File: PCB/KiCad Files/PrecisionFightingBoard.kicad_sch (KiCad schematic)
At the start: 14 parts, among them J1 Conn_01x04_Male, J10 ST01x05, J2 Screw_Terminal_01x04, J3 Conn_01x14_Socket, J4 Conn_01x14_Socket, J6 Conn_02x10_Odd_Even, J7 ST01x05, J8 ST01x05, J9 ST01x05, U1 Teensy4.0

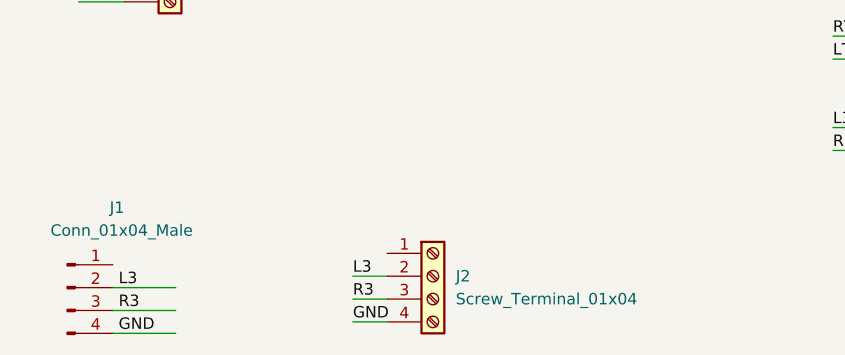
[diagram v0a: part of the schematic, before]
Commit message: Changed 4-pin screw terminal to 3-pin.
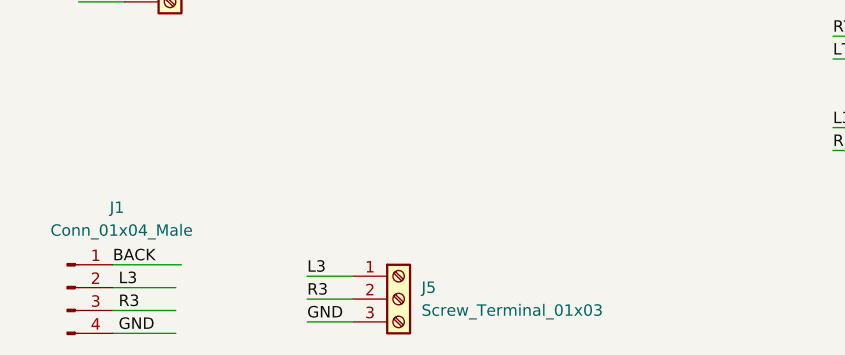
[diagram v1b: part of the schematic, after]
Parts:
- removed J2: Screw_Terminal_01x04, TerminalBlock_MetzConnect:TerminalBlock_MetzConnect_Type059_RT06304HBWC_1x04_P3.50mm_Horizontal, symbol Connector:Screw_Terminal_01x04
- added J5: Screw_Terminal_01x03, symbol Connector:Screw_Terminal_01x03
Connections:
- net BACK: now also J1.1 (Pin_1)
- net GND: now also J5.3 (Pin_3)
- net L3: now also J5.1 (Pin_1)
- net R3: now also J5.2 (Pin_2)
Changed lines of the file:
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@@
     (stroke (width 0) (type default))
   )
-  (wire (pts (xy 60.96 102.87) (xy 64.77 102.87))
+  (wire (pts (xy 55.88 102.87) (xy 60.96 102.87))
     (stroke (width 0) (type default))
   )
@@
     (stroke (width 0) (type default))
   )
+  (wire (pts (xy 55.88 100.33) (xy 60.96 100.33))
+    (stroke (width 0) (type default))
+  )
   (wire (pts (xy 92.71 40.64) (xy 85.09 40.64))
     (stroke (width 0) (type default))
@@
     (stroke (width 0) (type default))
   )
+  (wire (pts (xy 55.88 105.41) (xy 60.96 105.41))
+    (stroke (width 0) (type default))
+  )
   (wire (pts (xy 63.5 45.72) (xy 72.39 45.72))
     (stroke (width 0) (type default))
@@
     (stroke (width 0) (type default))
   )
+  (wire (pts (xy 34.29 99.06) (xy 41.91 99.06))
+    (stroke (width 0) (type default))
+  )
   (wire (pts (xy 92.71 53.34) (xy 85.09 53.34))
     (stroke (width 0) (type default))
@@
     (stroke (width 0) (type default))
   )
-  (wire (pts (xy 60.96 100.33) (xy 64.77 100.33))
-    (stroke (width 0) (type default))
-  )
   (wire (pts (xy 35.56 69.85) (xy 30.48 69.85))
     (stroke (width 0) (type default))
@@
     (stroke (width 0) (type default))
   )
-  (wire (pts (xy 60.96 105.41) (xy 64.77 105.41))
-    (stroke (width 0) (type default))
-  )
   (label "START" (at 31.115 44.45 0) (fields_autoplaced)
     (effects (font (size 1.27 1.27)) (justify left bottom))
   )
+  (label "GND" (at 55.88 105.41 0) (fields_autoplaced)
+    (effects (font (size 1.27 1.27)) (justify left bottom))
+  )
   (label "X" (at 180.34 41.91 0) (fields_autoplaced)
     (effects (font (size 1.27 1.27)) (justify left bottom))
@@
     (effects (font (size 1.27 1.27)) (justify left bottom))
   )
+  (label "R3" (at 55.88 102.87 0) (fields_autoplaced)
+    (effects (font (size 1.27 1.27)) (justify left bottom))
+  )
   (label "DOWN" (at 180.34 26.67 0) (fields_autoplaced)
     (effects (font (size 1.27 1.27)) (justify left bottom))
@@
     (effects (font (size 1.27 1.27)) (justify left bottom))
   )
+  (label "BACK" (at 34.29 99.06 0) (fields_autoplaced)
+    (effects (font (size 1.27 1.27)) (justify left bottom))
+  )
   (label "RT" (at 213.36 52.07 0) (fields_autoplaced)
     (effects (font (size 1.27 1.27)) (justify left bottom))
@@
     (effects (font (size 1.27 1.27)) (justify left bottom))
   )
-  (label "R3" (at 60.96 102.87 0) (fields_autoplaced)
-    (effects (font (size 1.27 1.27)) (justify left bottom))
-  )
   (label "BACK" (at 114.3 38.1 0) (fields_autoplaced)
     (effects (font (size 1.27 1.27)) (justify left bottom))
@@
     (effects (font (size 1.27 1.27)) (justify left bottom))
   )
-  (label "L3" (at 60.96 100.33 0) (fields_autoplaced)
-    (effects (font (size 1.27 1.27)) (justify left bottom))
-  )
   (label "GND" (at 31.115 69.85 0) (fields_autoplaced)
     (effects (font (size 1.27 1.27)) (justify left bottom))
@@
     (effects (font (size 1.27 1.27)) (justify left bottom))
   )
-  (label "GND" (at 60.96 105.41 0) (fields_autoplaced)
-    (effects (font (size 1.27 1.27)) (justify left bottom))
-  )
   (label "START" (at 114.3 40.64 0) (fields_autoplaced)
     (effects (font (size 1.27 1.27)) (justify left bottom))
@@
   )
   (label "GND" (at 34.925 106.68 0) (fields_autoplaced)
+    (effects (font (size 1.27 1.27)) (justify left bottom))
+  )
+  (label "L3" (at 55.88 100.33 0) (fields_autoplaced)
     (effects (font (size 1.27 1.27)) (justify left bottom))
   )
@@
     )
   )
+  (symbol (lib_id "Connector:Screw_Terminal_01x03") (at 66.04 102.87 0) (unit 1)
+    (in_bom yes) (on_board yes) (dnp no) (fields_autoplaced)
+    (property "Reference" "J5" (at 68.58 101.6 0)
+      (effects (font (size 1.27 1.27)) (justify left))
+    )
+    (property "Value" "Screw_Terminal_01x03" (at 68.58 104.14 0)
+      (effects (font (size 1.27 1.27)) (justify left))
+    )
+    (property "Footprint" "" (at 66.04 102.87 0)
+      (effects (font (size 1.27 1.27)) hide)
+    )
+    (property "Datasheet" "~" (at 66.04 102.87 0)
+      (effects (font (size 1.27 1.27)) hide)
+    )
+    (pin "1")
+    (pin "2")
+    (pin "3")
+    (instances
+      (project "PrecisionFightingBoard"
+        (path "/01d790aa-01e7-46c4-a23c-7deb91137dd0"
+          (reference "J5") (unit 1)
+        )
+      )
+    )
+  )
   (symbol (lib_id "Connector:Conn_01x04_Male") (at 29.21 101.6 0) (unit 1)
     (in_bom yes) (on_board yes) (dnp no)
@@
         )
       )
-    )
-  )
-  (symbol (lib_id "Connector:Screw_Terminal_01x04") (at 69.85 100.33 0) (unit 1)
-    (in_bom yes) (on_board yes) (dnp no) (fields_autoplaced)
-    (property "Reference" "J2" (at 72.39 100.33 0)
-      (effects (font (size 1.27 1.27)) (justify left))
-    )
-    (property "Value" "Screw_Terminal_01x04" (at 72.39 102.87 0)
-      (effects (font (size 1.27 1.27)) (justify left))
-    )
-    (property "Footprint" "TerminalBlock_MetzConnect:TerminalBlock_MetzConnect_Type059_RT06304HBWC_1x04_P3.50mm_Horizontal" (at 69.85 100.33 0)
-      (effects (font (size 1.27 1.27)) hide)
-    )
-    (property "Datasheet" "~" (at 69.85 100.33 0)
-      (effects (font (size 1.27 1.27)) hide)
-    )
-    (pin "1")
-    (pin "2")
-    (pin "3")
-    (pin "4")
-    (instances
-      (project "PrecisionFightingBoard"
-        (path "/01d790aa-01e7-46c4-a23c-7deb91137dd0"
-          (reference "J2") (unit 1)
-        )
-      )

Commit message: Updated wiring.
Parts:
- J5: footprint (none) -> TerminalBlock_MetzConnect:TerminalBlock_MetzConnect_Type059_RT06303HBWC_1x03_P3.50mm_Horizontal
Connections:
- net 5V: no longer J7.1 (Pin_1)
- net GND: now also J7.1 (Pin_1)
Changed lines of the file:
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@@
-    (effects (font (size 1.27 1.27)) (justify left bottom))
-  )
-  (label "5V" (at 31.115 21.59 0) (fields_autoplaced)
     (effects (font (size 1.27 1.27)) (justify left bottom))
   )
@@
   )
   (label "LB" (at 31.115 54.61 0) (fields_autoplaced)
+    (effects (font (size 1.27 1.27)) (justify left bottom))
+  )
+  (label "GND" (at 30.48 21.59 0) (fields_autoplaced)
     (effects (font (size 1.27 1.27)) (justify left bottom))
   )
@@
       (effects (font (size 1.27 1.27)) (justify left))
     )
-    (property "Footprint" "" (at 66.04 102.87 0)
-      (effects (font (size 1.27 1.27)) hide)
-    )
+    (property "Footprint" "TerminalBlock_MetzConnect:TerminalBlock_MetzConnect_Type059_RT06303HBWC_1x03_P3.50mm_Horizontal" (at 66.04 102.87 0)
+      (effects (font (size 1.27 1.27)) hide)
+    )

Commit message: fix pcb
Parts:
- removed J3, J4: Conn_01x14_Socket, Connector_PinSocket_2.54mm:PinSocket_1x14_P2.54mm_Vertical, symbol Connector:Conn_01x14_Socket
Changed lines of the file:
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@@
-    (stroke (width 0) (type default))
-  )
-  (wire (pts (xy 180.34 41.91) (xy 185.42 41.91))
     (stroke (width 0) (type default))
   )
@@
     (stroke (width 0) (type default))
   )
-  (wire (pts (xy 180.34 26.67) (xy 185.42 26.67))
-    (stroke (width 0) (type default))
-  )
-  (wire (pts (xy 180.34 46.99) (xy 185.42 46.99))
-    (stroke (width 0) (type default))
-  )
   (wire (pts (xy 114.3 25.4) (xy 119.38 25.4))
     (stroke (width 0) (type default))
@@
     (stroke (width 0) (type default))
   )
-  (wire (pts (xy 180.34 36.83) (xy 185.42 36.83))
-    (stroke (width 0) (type default))
-  )
   (wire (pts (xy 92.71 55.88) (xy 85.09 55.88))
     (stroke (width 0) (type default))
@@
     (stroke (width 0) (type default))
   )
-  (wire (pts (xy 213.36 52.07) (xy 218.44 52.07))
-    (stroke (width 0) (type default))
-  )
   (wire (pts (xy 92.71 48.26) (xy 85.09 48.26))
     (stroke (width 0) (type default))
@@
     (stroke (width 0) (type default))
   )
-  (wire (pts (xy 180.34 24.13) (xy 185.42 24.13))
-    (stroke (width 0) (type default))
-  )
   (wire (pts (xy 114.3 22.86) (xy 119.38 22.86))
     (stroke (width 0) (type default))
@@
     (stroke (width 0) (type default))
   )
-  (wire (pts (xy 180.34 39.37) (xy 185.42 39.37))
-    (stroke (width 0) (type default))
-  )
   (wire (pts (xy 63.5 55.88) (xy 72.39 55.88))
     (stroke (width 0) (type default))
@@
     (stroke (width 0) (type default))
   )
-  (wire (pts (xy 180.34 29.21) (xy 185.42 29.21))
-    (stroke (width 0) (type default))
-  )
-  (wire (pts (xy 180.34 44.45) (xy 185.42 44.45))
-    (stroke (width 0) (type default))
-  )
   (wire (pts (xy 35.56 26.67) (xy 30.48 26.67))
     (stroke (width 0) (type default))
   )
-  (wire (pts (xy 180.34 52.07) (xy 185.42 52.07))
-    (stroke (width 0) (type default))
-  )
-  (wire (pts (xy 180.34 54.61) (xy 185.42 54.61))
-    (stroke (width 0) (type default))
-  )
   (wire (pts (xy 114.3 40.64) (xy 119.38 40.64))
     (stroke (width 0) (type default))
@@
     (stroke (width 0) (type default))
   )
-  (wire (pts (xy 213.36 49.53) (xy 218.44 49.53))
-    (stroke (width 0) (type default))
-  )
   (wire (pts (xy 35.56 39.37) (xy 30.48 39.37))
     (stroke (width 0) (type default))
@@
     (stroke (width 0) (type default))
   )
-  (wire (pts (xy 180.34 34.29) (xy 185.42 34.29))
-    (stroke (width 0) (type default))
-  )
   (wire (pts (xy 63.5 48.26) (xy 72.39 48.26))
     (stroke (width 0) (type default))
@@
     (stroke (width 0) (type default))
   )
-  (wire (pts (xy 180.34 31.75) (xy 185.42 31.75))
-    (stroke (width 0) (type default))
-  )
   (wire (pts (xy 92.71 58.42) (xy 85.09 58.42))
     (stroke (width 0) (type default))
@@
     (stroke (width 0) (type default))
   )
-  (wire (pts (xy 180.34 49.53) (xy 185.42 49.53))
-    (stroke (width 0) (type default))
-  )
   (wire (pts (xy 92.71 43.18) (xy 85.09 43.18))
     (stroke (width 0) (type default))
@@
     (stroke (width 0) (type default))
   )
-  (wire (pts (xy 213.36 39.37) (xy 218.44 39.37))
-    (stroke (width 0) (type default))
-  )
   (wire (pts (xy 35.56 59.69) (xy 30.48 59.69))
     (stroke (width 0) (type default))
@@
     (stroke (width 0) (type default))
   )
-  (wire (pts (xy 180.34 21.59) (xy 185.42 21.59))
-    (stroke (width 0) (type default))
-  )
   (wire (pts (xy 114.3 35.56) (xy 119.38 35.56))
     (stroke (width 0) (type default))
@@
     (stroke (width 0) (type default))
   )
-  (wire (pts (xy 213.36 41.91) (xy 218.44 41.91))
-    (stroke (width 0) (type default))
-  )
   (wire (pts (xy 35.56 62.23) (xy 30.48 62.23))
     (stroke (width 0) (type default))
@@
     (effects (font (size 1.27 1.27)) (justify left bottom))
   )
-  (label "X" (at 180.34 41.91 0) (fields_autoplaced)
-    (effects (font (size 1.27 1.27)) (justify left bottom))
-  )
   (label "GND" (at 31.115 36.83 0) (fields_autoplaced)
     (effects (font (size 1.27 1.27)) (justify left bottom))
@@
     (effects (font (size 1.27 1.27)) (justify left bottom))
   )
-  (label "BACK" (at 180.34 36.83 0) (fields_autoplaced)
-    (effects (font (size 1.27 1.27)) (justify left bottom))
-  )
   (label "LEFT" (at 114.3 30.48 0) (fields_autoplaced)
     (effects (font (size 1.27 1.27)) (justify left bottom))
@@
     (effects (font (size 1.27 1.27)) (justify left bottom))
   )
-  (label "RB" (at 180.34 46.99 0) (fields_autoplaced)
-    (effects (font (size 1.27 1.27)) (justify left bottom))
-  )
   (label "R3" (at 55.88 102.87 0) (fields_autoplaced)
     (effects (font (size 1.27 1.27)) (justify left bottom))
   )
-  (label "DOWN" (at 180.34 26.67 0) (fields_autoplaced)
-    (effects (font (size 1.27 1.27)) (justify left bottom))
-  )
   (label "GND" (at 85.725 38.1 0) (fields_autoplaced)
     (effects (font (size 1.27 1.27)) (justify left bottom))
@@
     (effects (font (size 1.27 1.27)) (justify left bottom))
   )
-  (label "RT" (at 213.36 52.07 0) (fields_autoplaced)
-    (effects (font (size 1.27 1.27)) (justify left bottom))
-  )
-  (label "GND" (at 180.34 21.59 0) (fields_autoplaced)
-    (effects (font (size 1.27 1.27)) (justify left bottom))
-  )
-  (label "START" (at 180.34 39.37 0) (fields_autoplaced)
-    (effects (font (size 1.27 1.27)) (justify left bottom))
-  )
-  (label "HOME" (at 180.34 34.29 0) (fields_autoplaced)
-    (effects (font (size 1.27 1.27)) (justify left bottom))
-  )
   (label "LT" (at 114.3 76.2 0) (fields_autoplaced)
     (effects (font (size 1.27 1.27)) (justify left bottom))
   )
-  (label "R3" (at 213.36 39.37 0) (fields_autoplaced)
-    (effects (font (size 1.27 1.27)) (justify left bottom))
-  )
-  (label "L3" (at 213.36 41.91 0) (fields_autoplaced)
-    (effects (font (size 1.27 1.27)) (justify left bottom))
-  )
-  (label "RIGHT" (at 180.34 31.75 0) (fields_autoplaced)
-    (effects (font (size 1.27 1.27)) (justify left bottom))
-  )
   (label "RB" (at 69.215 48.26 0) (fields_autoplaced)
     (effects (font (size 1.27 1.27)) (justify left bottom))
   )
-  (label "Y" (at 180.34 44.45 0) (fields_autoplaced)
-    (effects (font (size 1.27 1.27)) (justify left bottom))
-  )
   (label "BACK" (at 85.725 53.34 0) (fields_autoplaced)
     (effects (font (size 1.27 1.27)) (justify left bottom))
@@
     (effects (font (size 1.27 1.27)) (justify left bottom))
   )
-  (label "LEFT" (at 180.34 29.21 0) (fields_autoplaced)
-    (effects (font (size 1.27 1.27)) (justify left bottom))
-  )
   (label "L3" (at 34.925 101.6 0) (fields_autoplaced)
     (effects (font (size 1.27 1.27)) (justify left bottom))
@@
     (effects (font (size 1.27 1.27)) (justify left bottom))
   )
-  (label "LT" (at 213.36 49.53 0) (fields_autoplaced)
-    (effects (font (size 1.27 1.27)) (justify left bottom))
-  )
   (label "LB" (at 31.115 54.61 0) (fields_autoplaced)
     (effects (font (size 1.27 1.27)) (justify left bottom))
@@
     (effects (font (size 1.27 1.27)) (justify left bottom))
   )
-  (label "LB" (at 180.34 49.53 0) (fields_autoplaced)
-    (effects (font (size 1.27 1.27)) (justify left bottom))
-  )
   (label "RIGHT" (at 31.115 31.75 0) (fields_autoplaced)
     (effects (font (size 1.27 1.27)) (justify left bottom))
   )
-  (label "A" (at 180.34 52.07 0) (fields_autoplaced)
-    (effects (font (size 1.27 1.27)) (justify left bottom))
-  )
   (label "GND" (at 34.925 106.68 0) (fields_autoplaced)
     (effects (font (size 1.27 1.27)) (justify left bottom))
@@
     (effects (font (size 1.27 1.27)) (justify left bottom))
   )
-  (label "UP" (at 180.34 24.13 0) (fields_autoplaced)
-    (effects (font (size 1.27 1.27)) (justify left bottom))
-  )
   (label "LT" (at 31.115 67.31 0) (fields_autoplaced)
     (effects (font (size 1.27 1.27)) (justify left bottom))
@@
   )
   (label "DOWN" (at 114.3 27.94 0) (fields_autoplaced)
-    (effects (font (size 1.27 1.27)) (justify left bottom))
-  )
-  (label "B" (at 180.34 54.61 0) (fields_autoplaced)
     (effects (font (size 1.27 1.27)) (justify left bottom))
   )
@@
         )
       )
-    )
-  )
-  (symbol (lib_id "Connector:Conn_01x14_Socket") (at 190.5 36.83 0) (unit 1)
-    (in_bom yes) (on_board yes) (dnp no) (fields_autoplaced)
-    (property "Reference" "J3" (at 191.77 36.83 0)
-      (effects (font (size 1.27 1.27)) (justify left))
-    )
-    (property "Value" "Conn_01x14_Socket" (at 191.77 39.37 0)
-      (effects (font (size 1.27 1.27)) (justify left))
-    )
-    (property "Footprint" "Connector_PinSocket_2.54mm:PinSocket_1x14_P2.54mm_Vertical" (at 190.5 36.83 0)
-      (effects (font (size 1.27 1.27)) hide)
-    )
-    (property "Datasheet" "~" (at 190.5 36.83 0)
-      (effects (font (size 1.27 1.27)) hide)
-    )
-    (pin "1")
-    (pin "10")
-    (pin "11")
-    (pin "12")
-    (pin "13")
-    (pin "14")
-    (pin "2")
-    (pin "3")
-    (pin "4")
-    (pin "5")
-    (pin "6")
-    (pin "7")
-    (pin "8")
-    (pin "9")
-    (instances
-      (project "PrecisionFightingBoard"
-        (path "/01d790aa-01e7-46c4-a23c-7deb91137dd0"
-          (reference "J3") (unit 1)
-        )
-      )
-    )
-  )
-  (symbol (lib_id "Connector:Conn_01x14_Socket") (at 223.52 36.83 0) (unit 1)
-    (in_bom yes) (on_board yes) (dnp no) (fields_autoplaced)
-    (property "Reference" "J4" (at 224.79 36.83 0)
-      (effects (font (size 1.27 1.27)) (justify left))
-    )
-    (property "Value" "Conn_01x14_Socket" (at 224.79 39.37 0)
-      (effects (font (size 1.27 1.27)) (justify left))
-    )
-    (property "Footprint" "Connector_PinSocket_2.54mm:PinSocket_1x14_P2.54mm_Vertical" (at 223.52 36.83 0)
-      (effects (font (size 1.27 1.27)) hide)
-    )
-    (property "Datasheet" "~" (at 223.52 36.83 0)
-      (effects (font (size 1.27 1.27)) hide)
-    )
-    (pin "1")
-    (pin "10")
-    (pin "11")
-    (pin "12")
-    (pin "13")
-    (pin "14")
-    (pin "2")
-    (pin "3")
-    (pin "4")
-    (pin "5")
-    (pin "6")
-    (pin "7")
-    (pin "8")
-    (pin "9")
-    (instances
-      (project "PrecisionFightingBoard"
-        (path "/01d790aa-01e7-46c4-a23c-7deb91137dd0"
-          (reference "J4") (unit 1)
-        )
-      )
